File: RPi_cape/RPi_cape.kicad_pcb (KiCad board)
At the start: 4 copper layers, 105 x 250 mm, 472 parts, among them J1 Conn_01x04, J10 Conn_01x02, J11 Conn_01x02, J12 Conn_01x02, J13 Conn_01x02, J14 Conn_01x02, J15 Conn_02x05_Odd_Even, J16 Conn_01x06, J2 Conn_01x02, J3 Conn_01x02, J4 Conn_01x02, J5 Conn_01x03, J6 Conn_01x03, J7 Conn_01x02, J8 Conn_02x20_Odd_Even, J9 Conn_01x02, Q1 NTD5865NLT4G, Q10 MMBT3904, Q11 MMBT3904, Q12 MMBT3906, Q13 MMBT3904, Q2 NTD5865NLT4G, Q3 NTD5865NLT4G, Q4 NTD5865NLT4G, Q5 MMBT3904, Q6 DNP, Q7 DNP, Q8 MMBT3904, Q9 MMBT3904, U1 TL431A, U11 LM2903, U12 LMC7101B, U13 LMC7101B, U17 LM2903, U18 74LVC1G08, U19 EL3H7(TA)-VG, U2 ADC128D818, U20 74LVC1G08, U21 EL3H7(TA)-VG, U22 74LVC1G08, U23 EL3H7(TA)-VG, U24 TL431A, U25 LM2903, U26 MIC1557, U27 MIC1557, U28 LM4871M, U29 LP5907MFX-3.3, U3 ADC128D818, U30 LP5907MFX-1.8, U31 5M40ZE64, U32 MIC1557, U33 5M80ZT100 / 5M240ZT100, U34 LMZ14203, U35 LMZ14203, U4 AD8552A, U5 LM2903, U6 LMC7101B, U7 LMC7101B, U8 74LVC1G08, U9 EL3H7(TA)-VG

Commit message: Finished layout, minor design changes
Assigned CPLD pins
Finished routing PCB
Moved rotary encoder inputs to CPLD
Removed separate decoupling caps for smaller CPLD footprint due to routing constraints
Added pull-downs on CPLD inputs for each valve driver (R198 etc.)
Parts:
- removed C77, C78, C80, C81, C82, C83: 100nF 50V X7R, Capacitor_SMD:C_0603_1608Metric
- removed C84, C85: 1uF 16V X7R, Capacitor_SMD:C_0805_2012Metric
- added H1: #4/M3, MountingHole:MountingHole_3.2mm_M3_Pad_Via, F.Cu at (95.8, -4.25)
- added H2: #4/M3, MountingHole:MountingHole_3.2mm_M3_Pad_Via, F.Cu at (0.25, -4.25)
- added H3: #4/M3, MountingHole:MountingHole_3.2mm_M3_Pad_Via, F.Cu at (95.8, -250.8)
- added H4: #4/M3, MountingHole:MountingHole_3.2mm_M3_Pad_Via, F.Cu at (0.25, -250.8)
- added R198: 10K, Resistor_SMD:R_1206_3216Metric, F.Cu at (61.5, -126.8)
- added R199: 10K, Resistor_SMD:R_1206_3216Metric, F.Cu at (61.5, -102.0)
- added R200: 10K, Resistor_SMD:R_1206_3216Metric, F.Cu at (61.8, -76.8)
- added R201: 10K, Resistor_SMD:R_1206_3216Metric, F.Cu at (61.5, -51.8)
- moved R182 353.0 mm to (17.0, -211.2), turned to 270 degrees
- moved R181 348.9 mm to (23.5, -210.2), turned to 270 degrees
- moved R62 326.3 mm to (21.8, -225.0), turned to 180 degrees
- moved R64 325.0 mm to (14.8, -216.8)
- moved C32 323.2 mm to (22.2, -222.2), turned to 180 degrees
- moved U13 322.8 mm to (13.8, -210.8)
- moved D17 320.9 mm to (16.5, -219.5)
- moved C37 320.8 mm to (14.8, -205.2), turned to 180 degrees
- moved R61 318.8 mm to (16.2, -225.0), turned to 180 degrees
- moved D18 317.0 mm to (21.8, -219.5)
- moved C34 316.3 mm to (21.2, -213.8)
- moved U12 316.2 mm to (20.2, -210.8)
- moved C35 314.9 mm to (14.1, -213.8)
- moved C36 314.4 mm to (19.8, -205.2), turned to 180 degrees
- moved R68 314.2 mm to (14.8, -207.5), turned to 180 degrees
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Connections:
- J16 pad 3: /+3.3V_RPi -> +3V3
- J8 pad 17: /+3.3V_RPi -> Net-(J8-Pad17)
- J8 pad 36: /Enc_A -> Net-(J8-Pad36)
- J8 pad 38: /Enc_B -> Net-(J8-Pad38)
- J8 pad 40: /Enc_Sw -> Net-(J8-Pad40)
- R193 pad 2: /+3.3V_RPi -> +3V3
- R194 pad 2: /+3.3V_RPi -> +3V3
- U31 pad 10: Net-(U31-Pad10) -> /Pressure2_Lim_H_Alarm
- U31 pad 11: Net-(U31-Pad11) -> /Pressure2_Lim_L_Alarm
- U31 pad 12: Net-(U31-Pad12) -> /O2_Lim_H_Alarm
- U31 pad 13: Net-(U31-Pad13) -> /O2_Lim_L_Alarm
- U31 pad 24: Net-(U31-Pad24) -> /Comms1
- U31 pad 25: Net-(U31-Pad25) -> /Comms2
- U31 pad 26: Net-(U31-Pad26) -> /Comms3
- U31 pad 27: Net-(U31-Pad27) -> /Comms4
- U31 pad 28: Net-(U31-Pad28) -> /Comms5
- U31 pad 29: Net-(U31-Pad29) -> /Comms6
- U31 pad 3: Net-(U31-Pad3) -> /Pressure1_Lim_H_Alarm
- U31 pad 30: Net-(U31-Pad30) -> /RPi_En
- U31 pad 31: Net-(U31-Pad31) -> /CPLD_valve4
- U31 pad 32: Net-(U31-Pad32) -> /CPLD_valve3
- U31 pad 33: Net-(U31-Pad33) -> /CPLD_valve2
- U31 pad 34: Net-(U31-Pad34) -> /CPLD_valve1
- U31 pad 35: Net-(U31-Pad35) -> /Enc_Sw
- U31 pad 36: Net-(U31-Pad36) -> /Enc_B
- U31 pad 37: Net-(U31-Pad37) -> /Enc_A
- U31 pad 4: Net-(U31-Pad4) -> /Pressure1_Lim_L_Alarm
- U31 pad 43: Net-(U31-Pad43) -> /CPLD/Extra6
- U31 pad 44: Net-(U31-Pad44) -> /CPLD/Extra5
- U31 pad 45: Net-(U31-Pad45) -> /CPLD/Extra4
- U31 pad 46: Net-(U31-Pad46) -> /CPLD/Extra3
- U31 pad 47: Net-(U31-Pad47) -> /CPLD/Extra2
- U31 pad 48: Net-(U31-Pad48) -> /CPLD/Extra1
- U31 pad 49: Net-(U31-Pad49) -> /Auditory Alarm/Low_Bat
- U31 pad 50: Net-(U31-Pad50) -> /CPLD_Alarm_Spkr
- U31 pad 51: Net-(U31-Pad51) -> /CPLD/~ADC_INT
- U31 pad 58: Net-(U31-Pad58) -> /CPLD_SCL
- U31 pad 59: Net-(U31-Pad59) -> /CPLD/SCL_Drive
- U31 pad 63: Net-(U31-Pad63) -> /CPLD/SDA_Drive
- U31 pad 64: Net-(U31-Pad64) -> /CPLD_SDA
- U31 pad 7: Net-(U31-Pad7) -> /CPLD/CPLD_Clk
- U33 pad 100: Net-(U33-Pad100) -> /CPLD_SDA
- U33 pad 12: Net-(U33-Pad12) -> /CPLD/CPLD_Clk
- U33 pad 18: Net-(U33-Pad18) -> /Pressure2_Lim_H_Alarm
- U33 pad 19: Net-(U33-Pad19) -> /Pressure2_Lim_L_Alarm
- U33 pad 20: Net-(U33-Pad20) -> /O2_Lim_H_Alarm
- U33 pad 21: Net-(U33-Pad21) -> /O2_Lim_L_Alarm
- U33 pad 35: Net-(U33-Pad35) -> /Comms1
- U33 pad 36: Net-(U33-Pad36) -> /Comms2
- U33 pad 37: Net-(U33-Pad37) -> /Comms3
- U33 pad 39: Net-(U33-Pad39) -> /Comms4
- U33 pad 4: Net-(U33-Pad4) -> /Pressure1_Lim_H_Alarm
- U33 pad 40: Net-(U33-Pad40) -> /Comms5
- U33 pad 41: Net-(U33-Pad41) -> /Comms6
- U33 pad 42: Net-(U33-Pad42) -> /RPi_En
- U33 pad 48: Net-(U33-Pad48) -> /CPLD_valve4
- U33 pad 49: Net-(U33-Pad49) -> /CPLD_valve3
- U33 pad 5: Net-(U33-Pad5) -> /Pressure1_Lim_L_Alarm
- U33 pad 50: Net-(U33-Pad50) -> /CPLD_valve2
- U33 pad 51: Net-(U33-Pad51) -> /CPLD_valve1
- U33 pad 53: Net-(U33-Pad53) -> /Enc_Sw
- U33 pad 54: Net-(U33-Pad54) -> /Enc_B
- U33 pad 55: Net-(U33-Pad55) -> /Enc_A
- U33 pad 68: Net-(U33-Pad68) -> /CPLD/Extra6
- U33 pad 69: Net-(U33-Pad69) -> /CPLD/Extra5
- U33 pad 70: Net-(U33-Pad70) -> /CPLD/Extra4
- U33 pad 71: Net-(U33-Pad71) -> /CPLD/Extra3
- U33 pad 72: Net-(U33-Pad72) -> /CPLD/Extra2
- U33 pad 73: Net-(U33-Pad73) -> /CPLD/Extra1
- U33 pad 74: Net-(U33-Pad74) -> /Auditory Alarm/Low_Bat
- U33 pad 75: Net-(U33-Pad75) -> /CPLD_Alarm_Spkr
- U33 pad 76: Net-(U33-Pad76) -> /CPLD/~ADC_INT
- U33 pad 89: Net-(U33-Pad89) -> /CPLD_SCL
- U33 pad 90: Net-(U33-Pad90) -> /CPLD/SCL_Drive
- U33 pad 99: Net-(U33-Pad99) -> /CPLD/SDA_Drive
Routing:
- net GND: track 81.0 -> 496.4 mm, vias 15 -> 214
- net +5VD: track 0.00 -> 341.4 mm, vias 0 -> 3
- net +24VA: track 1.81 -> 330.3 mm, vias 1 -> 4
- net +5V: track 0.00 -> 232.9 mm, vias 0 -> 3
- net /Pressure2_Lim_H_Alarm: track 0.00 -> 232.7 mm, vias 0 -> 3
- net +24V: track 0.00 -> 229.0 mm, vias 0 -> 17
- net /Pressure1_Lim_L_Alarm: track 5.45 -> 222.7 mm, vias 1 -> 2
- net /Pressure1_Lim_H_Alarm: track 4.53 -> 219.8 mm, vias 1 -> 2
- net /RPi_En: track 0.00 -> 208.4 mm, vias 0 -> 2
- net /+3.3V_RPi: track 0.00 -> 207.9 mm, vias 0 -> 4
- net /Pressure2_Lim_L_Alarm: track 0.00 -> 198.8 mm, vias 0 -> 2
- net /O2_Lim_H_Alarm: track 5.26 -> 199.5 mm, vias 1 -> 2
- net /RPi_SCL: track 0.00 -> 192.3 mm, vias 0 -> 2
- net /GPIO4: track 0.00 -> 190.9 mm, vias 0 -> 1
- net /RPi_SDA: track 0.00 -> 189.5 mm, vias 0 -> 2
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- added copper zone on In2.Cu, net +24V
- added copper zone on In2.Cu, net +3V3
- added copper zone on In2.Cu, net +5VA
- added copper zone on In2.Cu, net +BATT
- added copper zone on In2.Cu, net /+3.3V_RPi
- added copper zone on F.Cu, net GND
- added copper zone on In1.Cu, net GND
- added copper zone on In1.Cu, net GNDPWR
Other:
- board size 105 x 250 mm -> 104 x 255 mm
- net class Default: clearance 0.2 -> 0.16; trace_width 0.25 -> 0.2
- rule trace_clearance: 0.2 -> 0.16
- rule trace_min: 0.2 -> 0.18
- rule via_min_drill: 0.3 -> 0.254
- board text added: "#1"
- board text added: "#2"
- board text added: "#3"
- board text added: "#4"
- board text added: "+"
- board text added: "+1.8V"
- board text added: "+2.5V"
- board text added: "+24V"
- board text added: "+24VA"
- board text added: "+3.3V"
- board text added: "+5V"
- board text added: "+5V current"
- board text added: "+5V input current"
- board text added: "+5VA"
- board text added: "+5VD"
- board text added: "+5VD current"
- board text added: "+5VD input current"
- board text added: "-"
- board text added: "1"
- board text added: "100 kHz clk"
- board text added: "2"
- board text added: "3"
- board text added: "4"
- board text added: "5"
- board text added: "6"
- board text added: "Alarm Speaker"
- board text added: "CPLD"
- board text added: "GND"
- board text added: "GND PWR"
- board text added: "GNDPWR"
- board text added: "GPIO13"
- board text added: "GPIO18"
- board text added: "GPIO19"
- board text added: "GPIO26"
- board text added: "Gnd"
- board text added: "In"
- board text added: "JTAG for CPLD"
- board text added: "JamVent Stand-Alone Controller"
- board text added: "Low-Bat LED"
- board text added: "O2 Sensor"
- board text added: "Power"
- board text added: "Pressure Sensor 1"
- board text added: "Pressure Sensor 2"
- board text added: "RPi"
- board text added: "RPi +3.3V"
- board text added: "RPi +5VD"
- board text added: "Raspberry Pi"
- board text added: "Rotary Encoder"
- board text added: "SCL"
- board text added: "SDA"
- board text added: "V1.3, Don Straney 2020-04"
- board text added: "Valves"
- board text removed: "Misc. pull-ups to live near CPLD: re-arrange"
- board text removed: "Move near CPLD"

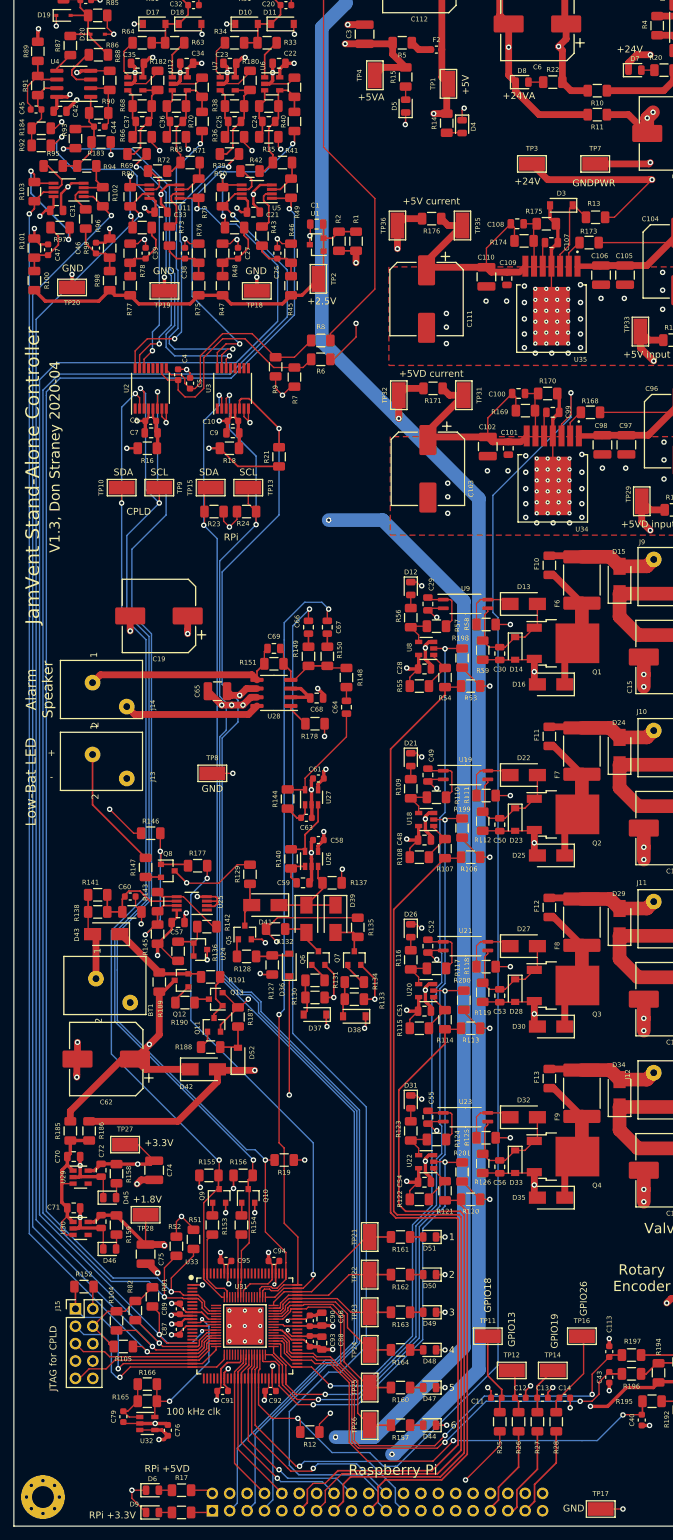
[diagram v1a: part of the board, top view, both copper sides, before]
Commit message: Digital pressure sensors
Added two digital pressure sensors each, on Raspberry Pi and CPLD I2C busses; preliminary layout only until mechanical details are finalized
Added gnd plane on bottom layer for heatsinking 5V regulators
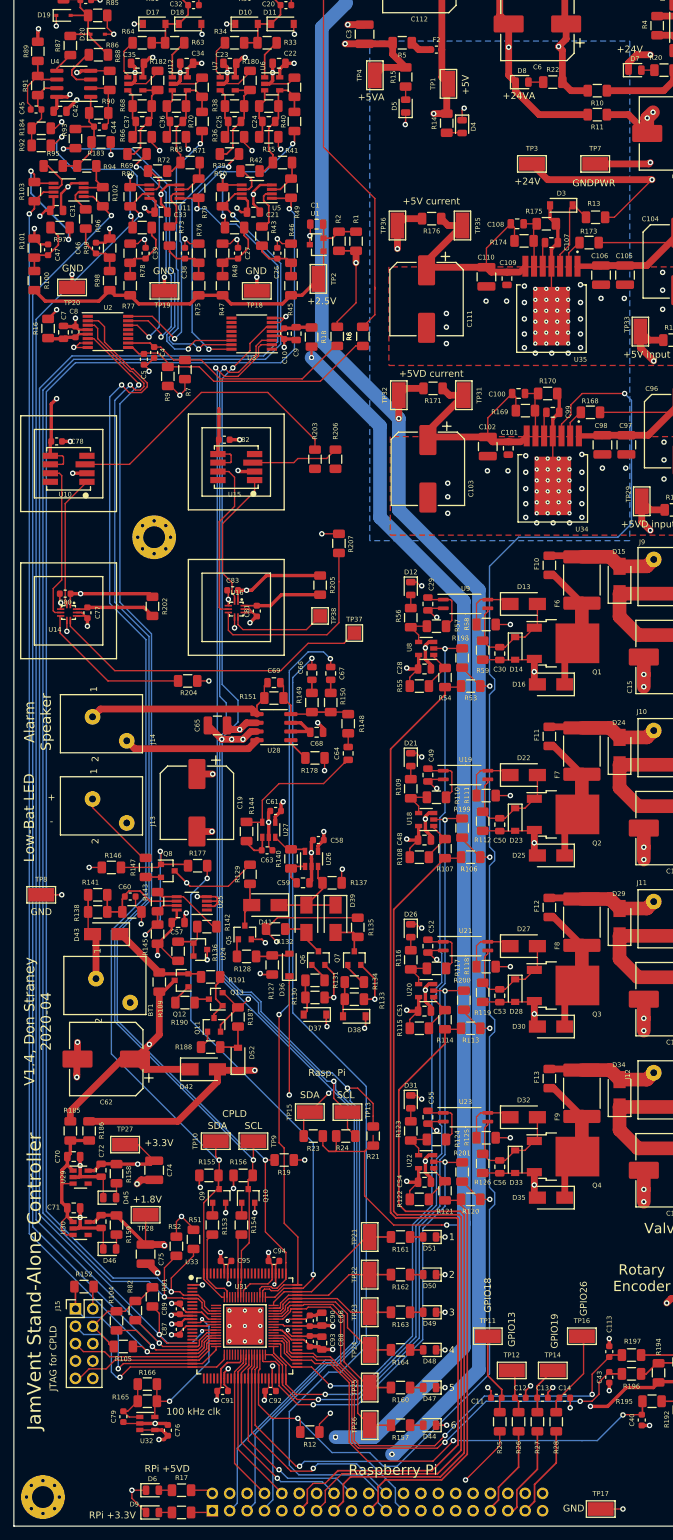
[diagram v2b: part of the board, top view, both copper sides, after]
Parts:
- added C77: 100nF 50V X7R, Capacitor_SMD:C_0603_1608Metric, F.Cu at (6.75, -133.5)
- added C78: 100nF 50V X7R, Capacitor_SMD:C_0603_1608Metric, F.Cu at (2.25, -158.5)
- added C80: 100nF 50V X7R, Capacitor_SMD:C_0603_1608Metric, F.Cu at (3.50, -136.2)
- added C81: 100nF 50V X7R, Capacitor_SMD:C_0603_1608Metric, F.Cu at (31.5, -133.7)
- added C82: 100nF 50V X7R, Capacitor_SMD:C_0603_1608Metric, F.Cu at (26.8, -158.8)
- added C83: 100nF 50V X7R, Capacitor_SMD:C_0603_1608Metric, F.Cu at (28.0, -136.8)
- added H5: #4/M3, MountingHole:MountingHole_3.2mm_M3_Pad_Via, F.Cu at (16.5, -144.5)
- added J17: Pressure_sensor_barb, Ventilator:Pressure_sensor_barb, F.Cu at (4.00, -133.8)
- added J18: Pressure_sensor_barb, Ventilator:Pressure_sensor_barb, F.Cu at (4.00, -155.2)
- added J19: Pressure_sensor_barb, Ventilator:Pressure_sensor_barb, F.Cu at (28.5, -134.2)
- added J20: Pressure_sensor_barb, Ventilator:Pressure_sensor_barb, F.Cu at (28.5, -155.5)
- added R202: 0, Resistor_SMD:R_1206_3216Metric, F.Cu at (16.2, -134.4)
- added R203: 0, Resistor_SMD:R_1206_3216Metric, F.Cu at (40.0, -155.9)
- added R204: 0, Resistor_SMD:R_1206_3216Metric, F.Cu at (21.4, -123.5)
- added R205: 0, Resistor_SMD:R_1206_3216Metric, F.Cu at (40.8, -137.5)
- added R206: 0, Resistor_SMD:R_1206_3216Metric, F.Cu at (43.0, -155.9)
- added R207: 0, Resistor_SMD:R_1206_3216Metric, F.Cu at (43.5, -143.6)
- added TP37: TestPoint, TestPoint:TestPoint_Pad_2.0x2.0mm, F.Cu at (45.8, -130.5)
- added TP38: TestPoint, TestPoint:TestPoint_Pad_2.0x2.0mm, F.Cu at (40.8, -133.0)
- added U10: MS5803-05BA, Ventilator:TE_MS5803-05BA, F.Cu at (4.00, -154.5)
- added U14: BMP388, Ventilator:Bosch_BMP388_HandSolder, F.Cu at (4.00, -133.5)
- added U15: MS5803-05BA, Ventilator:TE_MS5803-05BA, F.Cu at (28.5, -154.8)
- added U16: BMP388, Ventilator:Bosch_BMP388_HandSolder, F.Cu at (28.5, -134.0)
- moved R21 100.2 mm to (48.5, -57.0)
- moved TP10 96.5 mm to (25.5, -56.2)
- moved TP9 96.5 mm to (31.0, -56.2)
- moved R23 92.4 mm to (39.8, -57.0)
- moved R24 92.4 mm to (44.5, -57.0)
- moved TP13 92.4 mm to (44.8, -60.5)
- moved TP15 92.4 mm to (39.2, -60.5)
- moved TP8 30.7 mm to (0.00, -92.2)
- moved C19 27.9 mm to (22.8, -105.7), turned to 270 degrees
- moved R16 22.7 mm to (1.00, -175.0), turned to 90 degrees
- moved R18 20.2 mm to (39.5, -173.8), turned to 270 degrees
- moved C7 19.5 mm to (3.25, -174.4), turned to 270 degrees
- moved C9 17.2 mm to (37.2, -174.2), turned to 90 degrees
- moved C8 17.0 mm to (5.00, -174.5), turned to 270 degrees
- moved R7 16.0 mm to (21.0, -169.0)
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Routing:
- net /+3.3V_RPi: track 207.9 -> 277.6 mm, vias 4 -> 5
- net Net-(TP37-Pad1): track 0.00 -> 47.3 mm
- net /CPLD_SDA: track 150.5 -> 192.7 mm, vias 3 -> 2
- net Net-(R203-Pad1): track 0.00 -> 42.3 mm
- net /RPi_SDA: track 189.5 -> 227.8 mm
- net /RPi_SCL: track 192.3 -> 224.9 mm
- net /CPLD_SCL: track 154.0 -> 185.4 mm, vias 3 -> 2
- net Net-(R207-Pad1): track 0.00 -> 29.9 mm
- net GND: track 496.4 -> 523.5 mm, vias 214 -> 224
- net +3V3: track 167.5 -> 192.6 mm, vias 21 -> 24
- net Net-(R204-Pad1): track 0.00 -> 22.7 mm
- net /RPi_En: track 208.4 -> 229.5 mm
- net Net-(TP38-Pad1): track 0.00 -> 14.2 mm
- net Net-(R206-Pad1): track 0.00 -> 12.9 mm
- net +5VA: track 170.3 -> 182.8 mm, vias 15 -> 14
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- added copper zone on B.Cu, net GND
- removed copper zone on In2.Cu, net /+3.3V_RPi
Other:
- board text added: "Rasp. Pi"
- board text added: "V1.4, Don Straney 2020-04"
- board text removed: "RPi"
- board text removed: "V1.3, Don Straney 2020-04"

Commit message: Better valve monitoring, finalized layout and manufacturing files
Created assembly and fabrication drawings, assigned all BOM parts, generally made design ready for ordering
Added strain-relief slots and barb mounting dimensions for digital pressure sensors
Changed valve drivers from discrete power MOSFETs to "smart" industrial/automotive driver ICs for the current monitoring, including valve-movement monitor for #4
Connected RPi_Valve* signals to larger CPLD footprint, changed Raspberry Pi pin assignment as a result to ease PCB routing
Updated footprints, page layout to create readable assembly drawing
Added current-measurement testpoints for CPLD power from BATT+
Changed power diodes in power-down-alarm circuit to small-signal parts for more compact layout
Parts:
- removed D14, D23, D28, D33: 10V, Diode_SMD:D_SOD-123
- removed D22, D27, D32: ES2B, Diode_SMD:D_SMA
- removed F6, F7, F8, F9: 500mA 30V, Fuse:Fuse_2920_7451Metric
- removed H5: #4/M3, MountingHole:MountingHole_3.2mm_M3_Pad_Via
- removed J15: Conn_02x05_Odd_Even, Connector_PinHeader_2.54mm:PinHeader_2x05_P2.54mm_Vertical
- removed Q2, Q3, Q4: NTD5865NLT4G, Package_TO_SOT_SMD:TO-252-2
- added C84: 10nF 50V NP0, Capacitor_SMD:C_0603_1608Metric, F.Cu at (71.5, 233.3)
- added P15: Conn_02x05_Odd_Even, Connector_PinHeader_2.54mm:PinHeader_2x05_P2.54mm_Vertical, F.Cu at (37.5, 251.8)
- added R208: 10K, Resistor_SMD:R_1206_3216Metric, F.Cu at (83.9, 193.2)
- added R209: 1.5K, Resistor_SMD:R_1206_3216Metric, F.Cu at (108.0, 192.6)
- added R210: 2.4K, Resistor_SMD:R_1206_3216Metric, F.Cu at (110.5, 191.5)
- added R211: 10K, Resistor_SMD:R_1206_3216Metric, F.Cu at (73.5, 232.8)
- added R212: DNP, Resistor_SMD:R_1206_3216Metric, F.Cu at (86.2, 222.8)
- added R213: 10K, Resistor_SMD:R_1206_3216Metric, F.Cu at (84.1, 219.2)
- added R214: 1.5K, Resistor_SMD:R_1206_3216Metric, F.Cu at (107.8, 217.5)
- added R215: 2.4K, Resistor_SMD:R_1206_3216Metric, F.Cu at (110.2, 216.5)
- added R216: 1K, Resistor_SMD:R_1206_3216Metric, F.Cu at (76.0, 211.5)
- added R217: 100K, Resistor_SMD:R_1206_3216Metric, F.Cu at (78.5, 211.5)
- added R218: 100, Resistor_SMD:R_1206_3216Metric, F.Cu at (66.5, 205.2)
- added R219: 1M, Resistor_SMD:R_1206_3216Metric, F.Cu at (67.8, 210.5)
- added R220: 1K, Resistor_SMD:R_1206_3216Metric, F.Cu at (67.8, 213.0)
- added R221: 1M, Resistor_SMD:R_1206_3216Metric, F.Cu at (68.8, 216.5)
- added R222: 100K, Resistor_SMD:R_1206_3216Metric, F.Cu at (64.0, 221.5)
- added R223: 100K, Resistor_SMD:R_1206_3216Metric, F.Cu at (63.9, 224.2)
- added TP39: TestPoint_Flag, TestPoint:TestPoint_Keystone_5019_Minature, F.Cu at (66.0, 216.8)
- added TP40: TestPoint_Flag, TestPoint:TestPoint_Keystone_5019_Minature, F.Cu at (77.2, 216.0)
- added TP41: TestPoint_Flag, TestPoint:TestPoint_Keystone_5019_Minature, F.Cu at (67.8, 235.0)
- added TP42: TestPoint_Flag, TestPoint:TestPoint_Keystone_5019_Minature, F.Cu at (32.8, 222.0)
- added TP43: TestPoint_Flag, TestPoint:TestPoint_Keystone_5019_Minature, F.Cu at (33.0, 229.5)
- added U36: LMC7101B, Ventilator:SOT-23-5, F.Cu at (77.8, 205.0)
- added U37: LMC7101B, Ventilator:SOT-23-5, F.Cu at (71.8, 205.0)
- added U38: LMC7101B, Ventilator:SOT-23-5, F.Cu at (72.2, 215.0)
- C29, C30, C49: value DNP -> 10nF 50V NP0; footprint Capacitor_SMD:C_0805_2012Metric -> Capacitor_SMD:C_0603_1608Metric
- C50: value DNP -> 1nF 50V NP0; footprint Capacitor_SMD:C_0805_2012Metric -> Capacitor_SMD:C_0603_1608Metric
- C52, C53, C56: value DNP -> 1uF 16V X7R
- C55: value DNP -> 100nF 50V X7R; footprint Capacitor_SMD:C_0805_2012Metric -> Capacitor_SMD:C_0603_1608Metric
- D1, D15, D16, D2, D24, D25, D29, D30, D34, D35, D42, D43: footprint Diode_SMD:D_SMA -> Ventilator:D_SMA
- D10, D11, D17, D18, D3, D36, D37, D38, D52: footprint Diode_SMD:D_SOD-123 -> Ventilator:D_SOD-123
- D12, D21, D26, D31, D4, D44, D45, D46, D47, D48, D49, D5, D50, D51, D6, D7, D8, D9: footprint LED_SMD:LED_0805_2012Metric -> Ventilator:LED_0805_2012Metric
- D13, D41: value ES2B -> BAS21AH; footprint Diode_SMD:D_SMA -> Ventilator:D_SOD-323
- D19, D20: footprint Diode_SMD:D_SOD-323 -> Ventilator:D_SOD-323
- D39, D40: value DNP -> BAS21AH; footprint Diode_SMD:D_SMA -> Ventilator:D_SOD-323
- F10, F11, F12, F13: value DNP -> 1A 63VDC
- J17, J18, J19, J20: footprint Ventilator:Pressure_sensor_barb -> Ventilator:Pressure_sensor_barb_inner-lip-expanded-slots
- Q1: value NTD5865NLT4G -> MMBT3904; footprint Package_TO_SOT_SMD:TO-252-2 -> Ventilator:SOT-23
- Q10, Q11, Q12, Q13, Q5, Q6, Q7, Q8, Q9, U1, U24: footprint Package_TO_SOT_SMD:SOT-23 -> Ventilator:SOT-23
- R100, R101, R45, R46, R47, R48, R75, R76, R77, R78, R98, R99: value TBD -> DNP (TBD)
- R110: value 430 -> 1.5K
- R111: value 10K -> 2.4K
- R117: value 430 -> DNP
- R119: value 10K -> 1.5K
- R124: value 430 -> 2.4K
- R126, R58, R8: value 10K -> DNP
- R198, R199, R200, R201: value 10K -> 1K
- R57: value 430 -> 10K
- R9: value 1K -> DNP
- U11, U17, U25, U5: footprint Package_SO:VSSOP-8_3.0x3.0mm_P0.65mm -> Ventilator:VSSOP-8_3.0x3.0mm_P0.65mm
- U12, U13, U18, U20, U22, U26, U27, U29, U30, U32, U6, U7, U8: footprint Package_TO_SOT_SMD:SOT-23-5 -> Ventilator:SOT-23-5
- U14, U16: footprint Ventilator:Bosch_BMP388_HandSolder -> Ventilator:Bosch_BMP388
- U19, U21, U23, U9: value EL3H7(TA)-VG -> TPS1H100B; footprint Package_SO:SOIC-4_4.55x2.6mm_P1.27mm -> Ventilator:TSSOP-14-1EP_4.4x5mm_P0.65mm
- U2, U3: footprint Package_SO:TSSOP-16_4.4x5mm_P0.65mm -> Ventilator:TSSOP-16_4.4x5mm_P0.65mm
- U28, U4: footprint Package_SO:SOIC-8_3.9x4.9mm_P1.27mm -> Ventilator:SOIC-8_3.9x4.9mm_P1.27mm
- U31: value 5M40ZE64 -> DNP (5M40ZE64)
- moved R57 370.6 mm to (73.6, 238.8)
- moved Q1 351.1 mm to (59.7, 221.8), turned to 270 degrees
- moved D13 338.5 mm to (68.8, 203.8), turned to 90 degrees
- moved R112 338.1 mm to (78.0, 234.8)
- moved C50 306.8 mm to (81.5, 204.0), turned to 0 degrees
- moved F10 302.8 mm to (110.2, 160.2), turned to 180 degrees
- moved F11 302.8 mm to (110.2, 185.2), turned to 180 degrees
- moved F12 302.8 mm to (110.2, 210.2), turned to 180 degrees
- moved F13 302.8 mm to (110.2, 235.2), turned to 180 degrees
- moved C15 299.8 mm to (124.8, 171.0), turned to 0 degrees
- moved D15 297.9 mm to (115.5, 158.0), turned to 270 degrees
- moved D24 297.9 mm to (115.5, 183.0), turned to 270 degrees
- moved D29 297.9 mm to (115.5, 208.0), turned to 270 degrees
- moved D34 297.9 mm to (115.5, 233.0), turned to 270 degrees
- moved J10 297.9 mm to (125.5, 181.8)
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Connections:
- C29 pad 2: Net-(C29-Pad2) -> /CPLD_ADC3
- C30 pad 1: GNDPWR -> GND
- C30 pad 2: Net-(C30-Pad2) -> /CPLD_ADC4
- C4 pad 2: /CPLD_ADC6 -> /CPLD_ADC7
- C49 pad 2: Net-(C49-Pad2) -> /CPLD_ADC5
- C5 pad 2: /CPLD_ADC7 -> /CPLD_ADC6
- C50 pad 1: GNDPWR -> GND
- C50 pad 2: Net-(C50-Pad2) -> /CPLD_ADC3
- C52 pad 2: Net-(C52-Pad2) -> +5VA
- C53 pad 1: GNDPWR -> GND
- C53 pad 2: Net-(C53-Pad2) -> +5VA
- C56 pad 1: GNDPWR -> GND
- C56 pad 2: Net-(C56-Pad2) -> +5VA
- D13 pad 2: Net-(C30-Pad2) -> Net-(D13-Pad2)
- D15 pad 1: +24V -> /Output Driver 1/OutH
- D16 pad 1: Net-(D16-Pad1) -> /Output Driver 1/OutH
- D24 pad 1: +24V -> /Output Driver 2/OutH
- D25 pad 1: Net-(D25-Pad1) -> /Output Driver 2/OutH
- D29 pad 1: +24V -> /Output Driver 3/OutH
- D30 pad 1: Net-(D30-Pad1) -> /Output Driver 3/OutH
- D34 pad 1: +24V -> /Output Driver 4/OutH
- D35 pad 1: Net-(D35-Pad1) -> /Output Driver 4/OutH
- F10 pad 2: Net-(D16-Pad1) -> GNDPWR
- F11 pad 2: Net-(D25-Pad1) -> GNDPWR
- F12 pad 2: Net-(D30-Pad1) -> GNDPWR
- F13 pad 2: Net-(D35-Pad1) -> GNDPWR
- J10 pad 1: +24V -> /Output Driver 2/OutL
- J10 pad 2: /Output Driver 2/OutL -> /Output Driver 2/OutH
- J11 pad 1: +24V -> /Output Driver 3/OutL
- J11 pad 2: /Output Driver 3/OutL -> /Output Driver 3/OutH
- J12 pad 1: +24V -> /Output Driver 4/OutL
- J12 pad 2: /Output Driver 4/OutL -> /Output Driver 4/OutH
- J8 pad 11: /RPi_valve1 -> /RPi_Alarm_Spkr
- J8 pad 13: /RPi_valve2 -> Net-(J8-Pad13)
- J8 pad 15: /RPi_valve3 -> Net-(J8-Pad15)
- J8 pad 19: /RPi_valve4 -> Net-(J8-Pad19)
- J8 pad 21: /RPi_Alarm_Spkr -> Net-(J8-Pad21)
- J8 pad 32: Net-(J8-Pad32) -> /RPi_valve4
- J8 pad 36: Net-(J8-Pad36) -> /RPi_valve3
- J8 pad 38: Net-(J8-Pad38) -> /RPi_valve2
- J8 pad 40: Net-(J8-Pad40) -> /RPi_valve1
- J9 pad 1: +24V -> /Output Driver 1/OutL
- J9 pad 2: /Output Driver 1/OutL -> /Output Driver 1/OutH
- Q1 pad 1: Net-(C30-Pad2) -> Net-(Q1-Pad1)
- Q1 pad 2: Net-(D16-Pad1) -> GND
- Q1 pad 3: GNDPWR -> Net-(Q1-Pad3)
- R110 pad 1: Net-(R109-Pad2) -> GND
- R110 pad 2: Net-(C49-Pad2) -> Net-(R110-Pad2)
- R111 pad 1: +24V -> GND
- R111 pad 2: Net-(D22-Pad1) -> Net-(R111-Pad2)
- R112 pad 1: Net-(C50-Pad2) -> +3V3
- R112 pad 2: GNDPWR -> /~Valve2_Fault
- R117 pad 1: Net-(R116-Pad2) -> /~Valve2_Fault
- R117 pad 2: Net-(C52-Pad2) -> Net-(R117-Pad2)
- R118 pad 1: +24V -> /CPLD_ADC5
- R118 pad 2: Net-(D27-Pad1) -> Net-(R117-Pad2)
- R119 pad 1: Net-(C53-Pad2) -> GND
- R119 pad 2: GNDPWR -> Net-(R117-Pad2)
- R124 pad 1: Net-(R123-Pad2) -> GND
- R124 pad 2: Net-(C55-Pad2) -> Net-(R124-Pad2)
- R125 pad 1: +24V -> +3V3
- R125 pad 2: Net-(D32-Pad1) -> /~Valve3_Fault
- R126 pad 1: Net-(C56-Pad2) -> /~Valve3_Fault
- R126 pad 2: GNDPWR -> Net-(R126-Pad2)
- R57 pad 1: Net-(R56-Pad2) -> +3V3
- R57 pad 2: Net-(C29-Pad2) -> /~Valve1_Fault
- R58 pad 1: +24V -> /~Valve1_Fault
- R58 pad 2: Net-(D13-Pad1) -> Net-(R110-Pad2)
- R59 pad 1: Net-(C30-Pad2) -> /CPLD_ADC6
- R59 pad 2: GNDPWR -> Net-(R110-Pad2)
- R6 pad 2: /CPLD_ADC6 -> /CPLD_ADC7
- R7 pad 1: /CPLD_ADC6 -> /CPLD_ADC7
- R8 pad 2: /CPLD_ADC7 -> /CPLD_ADC6
- R9 pad 1: /CPLD_ADC7 -> /CPLD_ADC6
- U19 pad 1: Net-(C49-Pad2) -> (no net)
- U19 pad 3: Net-(C50-Pad2) -> Net-(R109-Pad2)
- U19 pad 4: Net-(D22-Pad1) -> (no net)
- U21 pad 1: Net-(C52-Pad2) -> (no net)
- U21 pad 3: Net-(C53-Pad2) -> Net-(R116-Pad2)
- U21 pad 4: Net-(D27-Pad1) -> (no net)
- U23 pad 1: Net-(C55-Pad2) -> (no net)
- U23 pad 3: Net-(C56-Pad2) -> Net-(R123-Pad2)
- U23 pad 4: Net-(D32-Pad1) -> (no net)
- U31 pad 52: Net-(U31-Pad52) -> /~Valve1_Fault
- U31 pad 53: Net-(U31-Pad53) -> /~Valve2_Fault
- U31 pad 54: Net-(U31-Pad54) -> /~Valve3_Fault
- U31 pad 55: Net-(U31-Pad55) -> /~Valve4_Fault
- U33 pad 26: Net-(U33-Pad26) -> /RPi_valve4
- U33 pad 27: Net-(U33-Pad27) -> /RPi_valve3
- U33 pad 28: Net-(U33-Pad28) -> /RPi_valve2
- U33 pad 29: Net-(U33-Pad29) -> /RPi_valve1
- U33 pad 84: Net-(U33-Pad84) -> /~Valve1_Fault
- U33 pad 85: Net-(U33-Pad85) -> /~Valve2_Fault
- U33 pad 86: Net-(U33-Pad86) -> /~Valve3_Fault
- U33 pad 87: Net-(U33-Pad87) -> /~Valve4_Fault
- U9 pad 1: Net-(C29-Pad2) -> (no net)
- U9 pad 3: Net-(C30-Pad2) -> Net-(R56-Pad2)
- U9 pad 4: Net-(D13-Pad1) -> (no net)
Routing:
- net /CPLD_ADC3: track 0.00 -> 151.6 mm
- net /~Valve1_Fault: track 0.00 -> 125.1 mm, vias 0 -> 2
- net /CPLD_ADC4: track 0.00 -> 123.0 mm
- net /CPLD_ADC5: track 0.00 -> 96.1 mm
- net /~Valve2_Fault: track 0.00 -> 90.3 mm, vias 0 -> 2
- net /CPLD_ADC6: track 35.0 -> 116.1 mm
- net /+3.3V_RPi: track 277.6 -> 347.8 mm
- net /~Valve3_Fault: track 0.00 -> 67.5 mm, vias 0 -> 2
- net /CPLD_SCL: track 185.4 -> 243.6 mm, vias 2 -> 5
- net /~Valve4_Fault: track 0.00 -> 56.5 mm, vias 0 -> 2
- net /RPi_SCL: track 224.9 -> 276.1 mm, vias 2 -> 8
- net /CPLD_SDA: track 192.7 -> 240.1 mm, vias 2 -> 5
- net /RPi_SDA: track 227.8 -> 274.4 mm, vias 2 -> 4
- net /RPi_valve4: track 59.1 -> 100.9 mm, vias 0 -> 2
- net /RPi_valve3: track 99.8 -> 140.7 mm, vias 0 -> 2
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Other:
- outline, holes or cut-outs redrawn
- board text added: "2.50 mm"
- board text added: "2x"
- board text added: "2x R 1.00 mm"
- board text added: "4x"
- board text added: "4x D 3.2 mm"
- board text added: "4x Slot 10 x 3 mm"
- board text added: "4x Slot, 3 mm width"
- board text added: "6x R 3.25 mm"
- board text added: "8x R 0.25 mm"
- board text added: "CPLD current"
- board text added: "NOTES: 1. Assembly to meet IPC-A-610 Class 2 standards 2. Modules U14, U16 have special requirements, as listed in the included Bosch BMP388 Handling & Soldering Guidelines. Most important requirements are... a. must not be soldered using a vapor-phase process, b. hole in top of casing must be covered during any liquid or aerosol process (such as cleaning) by a piece of polyimide tape or similar,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"
- board text added: "V1.5, Don Straney 2020-04"
- board text removed: "V1.4, Don Straney 2020-04"
